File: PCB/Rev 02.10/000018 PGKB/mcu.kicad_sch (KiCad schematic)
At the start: 32 parts, among them U5 RP2040, Y1 12 MHz

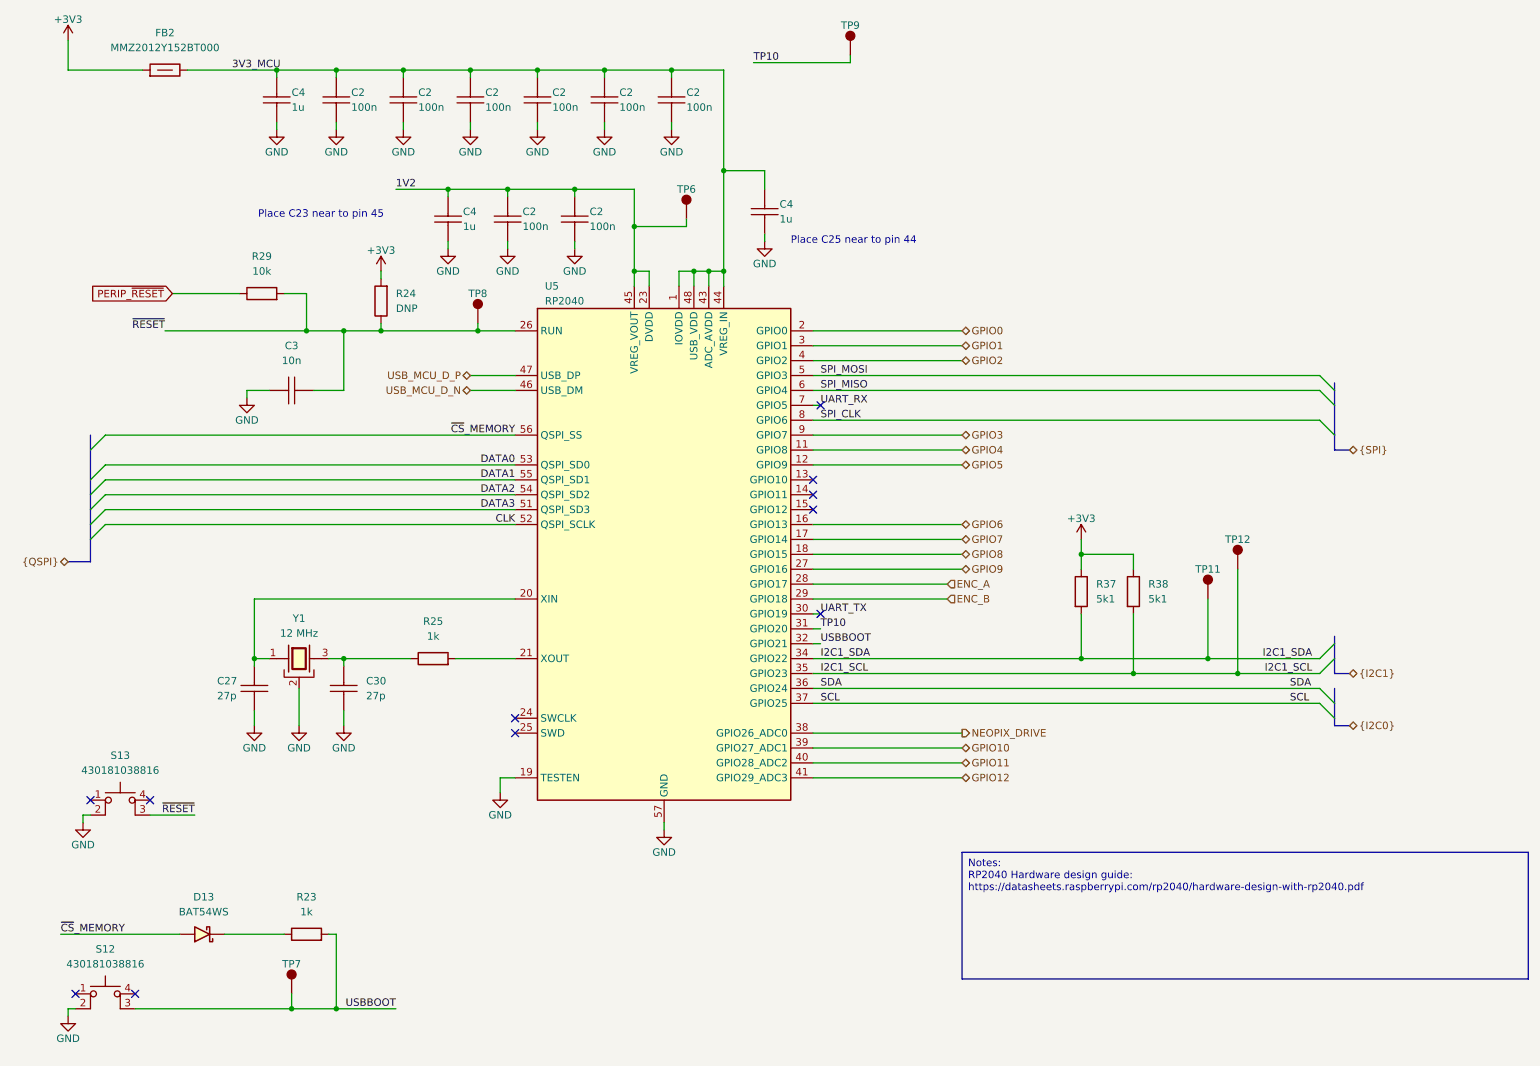
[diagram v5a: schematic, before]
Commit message: Resolved DRC problems
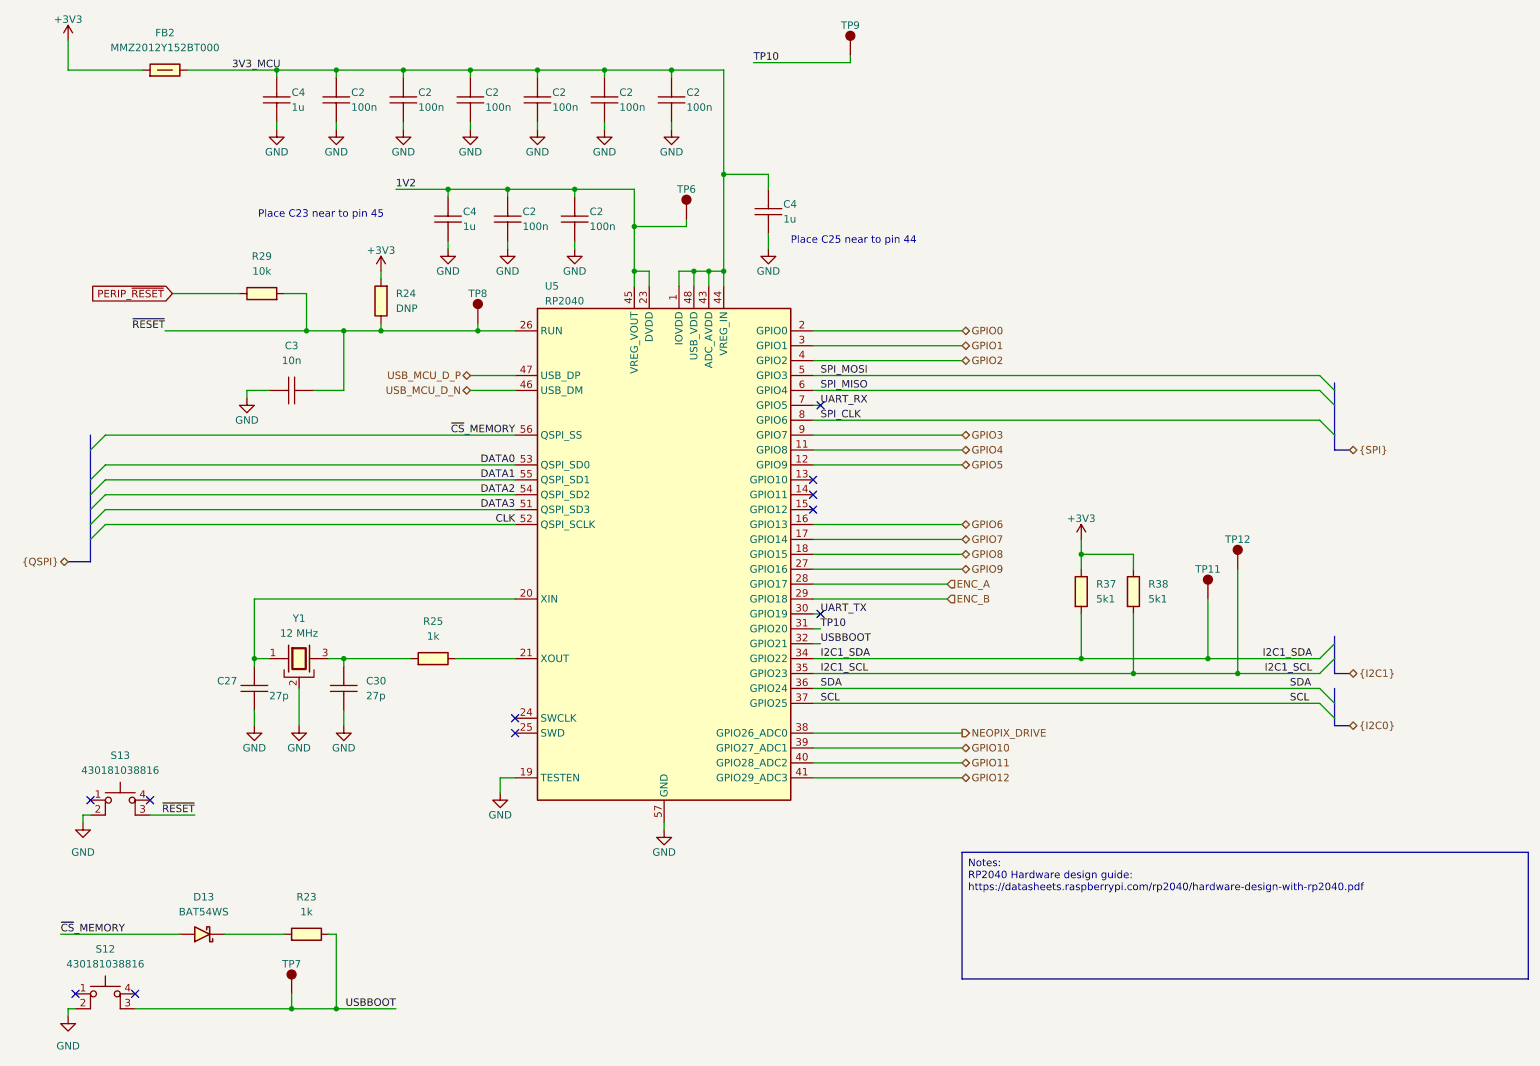
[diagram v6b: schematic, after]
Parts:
- C3: Code 10n -> (none)
- C4: Code 1u -> (none)
- FB2: value Ferrite_500mA_TDK_MMZ2012Y152BT000 -> MMZ2012Y152BT000; Code MMZ2012Y152BT000 -> (none)
- R23, R25: Code 1k -> (none)
- R29: Code 10k -> (none)
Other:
- moved on the sheet: C4

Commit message: Signals renamed
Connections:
- net GPIO3 is gone; now on net GPIO7: U5.9 (GPIO7)
- net GPIO4 is gone; now on net GPIO8: U5.11 (GPIO8)
- net GPIO5 is gone; now on net GPIO9: U5.12 (GPIO9)
- net GPIO7: no longer U5.17 (GPIO14)
- net GPIO8: no longer U5.18 (GPIO15)
- net GPIO9: no longer U5.27 (GPIO16)
- net GPIO10 renamed GPIO27
- net GPIO11 renamed GPIO28
- net GPIO12 renamed GPIO29
- net GPIO6 renamed GPIO13
- new net GPIO14: U5.17 (GPIO14)
- new net GPIO15: U5.18 (GPIO15)
- new net GPIO16: U5.27 (GPIO16)
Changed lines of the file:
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@@
 		)
 	)
-	(hierarchical_label "GPIO9"
+	(hierarchical_label "GPIO16"
 		(shape bidirectional)
 		(at 187.96 107.95 0)
@@
 		)
 	)
-	(hierarchical_label "GPIO11"
+	(hierarchical_label "GPIO28"
 		(shape bidirectional)
 		(at 187.96 140.97 0)
@@
 		)
 	)
-	(hierarchical_label "GPIO12"
+	(hierarchical_label "GPIO29"
 		(shape bidirectional)
 		(at 187.96 143.51 0)
@@
 		)
 	)
-	(hierarchical_label "GPIO5"
+	(hierarchical_label "GPIO9"
 		(shape bidirectional)
 		(at 187.96 90.17 0)
@@
 		)
 	)
-	(hierarchical_label "GPIO6"
+	(hierarchical_label "GPIO13"
 		(shape bidirectional)
 		(at 187.96 100.33 0)
@@
 		)
 	)
-	(hierarchical_label "GPIO8"
+	(hierarchical_label "GPIO15"
 		(shape bidirectional)
 		(at 187.96 105.41 0)
@@
 		)
 	)
-	(hierarchical_label "GPIO7"
+	(hierarchical_label "GPIO14"
 		(shape bidirectional)
 		(at 187.96 102.87 0)
@@
 		)
 	)
-	(hierarchical_label "GPIO4"
+	(hierarchical_label "GPIO8"
 		(shape bidirectional)
 		(at 187.96 87.63 0)
@@
 		)
 	)
-	(hierarchical_label "GPIO10"
+	(hierarchical_label "GPIO27"
 		(shape bidirectional)
 		(at 187.96 138.43 0)
@@
 		)
 	)
-	(hierarchical_label "GPIO3"
+	(hierarchical_label "GPIO7"
 		(shape bidirectional)
 		(at 187.96 85.09 0)
@@
 	)
 	(symbol
+		(lib_name "Button_tactile_45x38_430181038816_1")
 		(lib_id "KD_Switch:Button_tactile_45x38_430181038816")
 		(at 44.45 147.32 0)
